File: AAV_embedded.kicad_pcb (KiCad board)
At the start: 4 copper layers, 165.8 x 114.2 mm, 51 parts, among them J1 JTAG_SWD_CONN, J10 DRV_HIGH_C2, J11 DRV_LOW_C2, J12 DRV_HIGH_C3, J13 DRV_LOW_C3, J14 DRV_LOW_C1, J2 12v in, J3 USB_C_Receptacle_USB2.0_14P, J5 THR_EN_JMP, J6 GPIO_INTERNAL_PINS, J7 GPIO_EXT_PINS, J8 Conn_01x03_Pin, J9 DRV_HIGH_C1, SW1 DAC_ADDR, SW2 IO_EXT_ADDR, SW3 SW_DIP_x03, SW4 5v_USB_EN, SW5 DAC_EN, U1 DAC101C081CIMK, U2 PCA9555D, U3 LD1117S50TR_SOT223, U4 LD1117S33TR_SOT223, U5 FXMA108

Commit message: board layout v1
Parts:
- removed 12vdecoup_H1: 0.1uF, Capacitor_SMD:C_1206_3216Metric
- removed 12vdecoup_L1: 100uF, Capacitor_SMD:C_1206_3216Metric
- removed 3.3vreg_Cin1, 5vreg_Cin2: 100nF, Capacitor_SMD:C_1206_3216Metric
- removed 3.3vreg_Cout1, 5vreg_Cout2: 10uF, Capacitor_SMD:C_1206_3216Metric
- removed D1: D_Schottky_low_forward, Diode_SMD:D_1206_3216Metric
- removed R2: 2k, Resistor_SMD:R_1206_3216Metric
- removed S1: GPTS203211B, Button_Switch_SMD:SW_Push_1P1T_NO_CK_PTS125Sx43PSMTR
- removed U4: LD1117S33TR_SOT223, Package_TO_SOT_SMD:SOT-223-3_TabPin2
- added C3: 0.1uF, Capacitor_SMD:C_1206_3216Metric, F.Cu at (134.1, 97.5)
- added C4: 0.1uF, Capacitor_SMD:C_1206_3216Metric, F.Cu at (141.6, 123.4)
- added C5: 22pF, Capacitor_SMD:C_1206_3216Metric, F.Cu at (141.8, 112.3)
- added C6: 22pF, Capacitor_SMD:C_1206_3216Metric, F.Cu at (141.5, 120.2)
- added D4: LED, LED_SMD:LED_1206_3216Metric_Pad1.42x1.75mm_HandSolder, F.Cu at (153.8, 56.0)
- added D5: LED, LED_SMD:LED_1206_3216Metric_Pad1.42x1.75mm_HandSolder, F.Cu at (162.0, 104.8)
- added D6: LED, LED_SMD:LED_1206_3216Metric_Pad1.42x1.75mm_HandSolder, F.Cu at (161.9, 94.7)
- added F2: Polyfuse_3A_15V, Fuse:Fuse_1812_4532Metric, F.Cu at (65.1, 117.3)
- added J15: Brake/FwRev, Connector_PinHeader_2.54mm:PinHeader_1x03_P2.54mm_Horizontal, F.Cu at (202.8, 148.8)
- added J16: 5v_in, TerminalBlock_MetzConnect:TerminalBlock_MetzConnect_Type011_RT05502HBWC_1x02_P5.00mm_Horizontal, F.Cu at (73.7, 50.3)
- added J17: 3.3v_in, TerminalBlock_MetzConnect:TerminalBlock_MetzConnect_Type011_RT05502HBWC_1x02_P5.00mm_Horizontal, F.Cu at (85.2, 50.3)
- added J18: 12v_in, TerminalBlock_MetzConnect:TerminalBlock_MetzConnect_Type011_RT05502HBWC_1x02_P5.00mm_Horizontal, F.Cu at (96.9, 50.3)
- added J19: ~, SparkFun-Connectors:JST-2-PTH, F.Cu at (159.2, 155.5)
- added J20: ~, SparkFun-Connectors:JST-6-SMD-1.25MM-LOCKING, F.Cu at (145.5, 155.9)
- added J21: CAN, Connector_JST:JST_EH_B2B-EH-A_1x02_P2.50mm_Vertical, F.Cu at (152.6, 95.0)
- added J23: 5v_rail, Connector_PinHeader_2.54mm:PinHeader_1x05_P2.54mm_Vertical, F.Cu at (61.7, 46.4)
- added J24: 3.3v_rail, Connector_PinHeader_2.54mm:PinHeader_1x05_P2.54mm_Vertical, F.Cu at (57.1, 46.4)
- added J25: 12v_rail, Connector_PinHeader_2.54mm:PinHeader_1x05_P2.54mm_Vertical, F.Cu at (52.5, 46.4)
- added J26: GND_rail, Connector_PinHeader_2.54mm:PinHeader_1x05_P2.54mm_Vertical, F.Cu at (66.2, 46.1)
- added J27: 12v_rail_f, Connector_PinSocket_2.54mm:PinSocket_1x05_P2.54mm_Vertical, F.Cu at (52.3, 140.2)
- added J28: 3.3v_rail_f, Connector_PinSocket_2.54mm:PinSocket_1x05_P2.54mm_Vertical, F.Cu at (56.9, 140.2)
- added J29: 5v_rail_f, Connector_PinSocket_2.54mm:PinSocket_1x05_P2.54mm_Vertical, F.Cu at (61.5, 140.2)
- added J30: GND_rail_f, Connector_PinSocket_2.54mm:PinSocket_1x05_P2.54mm_Vertical, F.Cu at (66.1, 140.2)
- added JP1: CAN_TXD_SEL, Jumper:SolderJumper-3_P1.3mm_Bridged12_Pad1.0x1.5mm, F.Cu at (154.2, 106.5)
- added JP2: CAN_RXD_SEL, Jumper:SolderJumper-3_P1.3mm_Bridged12_Pad1.0x1.5mm, F.Cu at (148.7, 106.5)
- added R11: 2k, Resistor_SMD:R_1206_3216Metric, F.Cu at (122.5, 127.4)
- added R12: 2k, Resistor_SMD:R_1206_3216Metric, F.Cu at (122.7, 131.9)
- added R13: 2k, Resistor_SMD:R_1206_3216Metric, F.Cu at (135.7, 131.1)
- added R14: 2k, Resistor_SMD:R_1206_3216Metric, F.Cu at (135.8, 136.3)
- added R25: 10k, Resistor_SMD:R_1206_3216Metric, F.Cu at (153.9, 69.0)
- added R26: 10k, Resistor_SMD:R_1206_3216Metric, F.Cu at (153.7, 58.4)
- added R27: 10k, Resistor_SMD:R_1206_3216Metric, F.Cu at (162.0, 102.4)
- added R28: 10k, Resistor_SMD:R_1206_3216Metric, F.Cu at (161.9, 97.0)
- added SW6: ~{RESET_uMOD}, Button_Switch_SMD:SW_Push_SPST_NO_Alps_SKRK, F.Cu at (131.2, 48.6)
- added SW7: ~{BOOT_uMOD}, Button_Switch_SMD:SW_Push_SPST_NO_Alps_SKRK, F.Cu at (123.7, 48.9)
- added SW8: ~{RESET_BRK}, Button_Switch_SMD:SW_Push_SPST_NO_Alps_SKRK, F.Cu at (115.8, 48.9)
- added SW9: ~{RESET_STR}, Button_Switch_SMD:SW_Push_SPST_NO_Alps_SKRK, F.Cu at (108.1, 48.9)
- added U6: MCP2515-xSO, Package_SO:SOIC-18W_7.5x11.6mm_P1.27mm, F.Cu at (152.3, 116.6)
- added U7: SN65HVD230, Package_SO:SOIC-8_3.9x4.9mm_P1.27mm, F.Cu at (142.2, 96.8)
- added Y1: 16MHz, Crystal:Crystal_HC18-U_Vertical, F.Cu at (133.5, 118.0)
- D2: value D_TVS -> LED; footprint Diode_SMD:D_1206_3216Metric -> LED_SMD:LED_1206_3216Metric_Pad1.42x1.75mm_HandSolder
- D3: footprint LED_SMD:LED_1206_3216Metric -> LED_SMD:LED_1206_3216Metric_Pad1.42x1.75mm_HandSolder
- J2: value 12v in -> Raspberry_Pi_4; footprint Connector_PinSocket_1.00mm:PinSocket_1x02_P1.00mm_Vertical -> Connector_PinSocket_2.54mm:PinSocket_2x20_P2.54mm_Vertical
- J6: value GPIO_INTERNAL_PINS -> Conn_01x07; footprint Connector_PinHeader_2.54mm:PinHeader_1x09_P2.54mm_Vertical -> Connector_PinHeader_2.54mm:PinHeader_1x07_P2.54mm_Vertical
- J7: value GPIO_EXT_PINS -> Conn_01x05; footprint Connector_PinHeader_2.54mm:PinHeader_1x13_P2.54mm_Horizontal -> Connector_PinHeader_2.54mm:PinHeader_1x05_P2.54mm_Vertical
- J8: value Conn_01x03_Pin -> Throttle Connector
- R1: value 2k -> 10k
- SW5: value DAC_EN -> THR_EN
- U3: value LD1117S50TR_SOT223 -> 74AHC1G08; footprint Package_TO_SOT_SMD:SOT-223-3_TabPin2 -> Package_TO_SOT_SMD:SOT-23-5_HandSoldering
- moved C1 117.1 mm to (183.8, 135.3), turned to 180 degrees
- moved C2 117.0 mm to (182.7, 140.8), turned to -90 degrees
- moved R3 86.1 mm to (164.6, 143.2)
- moved J1 76.5 mm to (141.9, 72.0), turned to 90 degrees
- moved U3 73.8 mm to (150.7, 86.2), turned to 180 degrees
- moved R1 70.2 mm to (161.8, 112.7), turned to 180 degrees
- moved J4 57.6 mm to (126.5, 85.1)
- moved SW4 56.7 mm to (90.1, 151.2), turned to -90 degrees
- moved SW2 54.9 mm to (116.9, 117.3), turned to -90 degrees
- moved R7 53.1 mm to (98.2, 136.3)
- moved D2 51.4 mm to (153.9, 71.5)
- moved R6 51.0 mm to (98.1, 130.9)
- moved R8 43.2 mm to (73.1, 140.7), turned to -90 degrees
- moved R5 40.2 mm to (98.2, 133.7)
- moved J2 24.4 mm to (53.8, 119.9), turned to 180 degrees
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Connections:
- net RST renamed ~{RESET_uMOD}
- D2 pad 1: Net-(D1-A) -> GND
- D2 pad 2: GND -> Net-(D2-A)
- J14 pad 1: ERR_LOW -> ERR_BRK
- J14 pad 2: ~{RST_LOW} -> ~{RST_BRK}
- J14 pad 6: TX_LOW_5v -> TX_BRK_5v
- J14 pad 7: RX_LOW_5v -> RX_DRV_5v
- J14 pad 9: 5v_reg_LOW -> 5v_reg_BRK
- J2 pad 1: GND -> Net-(J2-3V3-Pad1)
- J2 pad 2: Net-(D1-A) -> Net-(F2-Pad1)
- J4 pad 11: unconnected-(J4-~{BOOT}-Pad11) -> ~{BOOT_uMOD}
- J4 pad 17: unconnected-(J4-TX1-Pad17) -> uMod_TX1
- J4 pad 19: unconnected-(J4-RX1-Pad19) -> uMod_RX1
- J4 pad 2: Net-(J4-3.3V-Pad2) -> +3.3V
- J4 pad 20: unconnected-(J4-RX2-Pad20) -> TX_DRV_L
- J4 pad 22: unconnected-(J4-TX2-Pad22) -> RX_DRV_L
- J4 pad 40: GPIO_INTERNAL_0 -> ~{E-STOP}
- J4 pad 41: unconnected-(J4-CAN-RX-Pad41) -> CAN_RXD
- J4 pad 42: GPIO_INTERNAL_1 -> ERR_L
- J4 pad 43: unconnected-(J4-CAN-TX-Pad43) -> CAN_TXD
- J4 pad 44: GPIO_INTERNAL_2 -> ~{E-STOP-TRIG}
- J4 pad 51: SDA _MCTRL_L -> unconnected-(J4-I2C_SDA1-Pad51)
- J4 pad 53: SCL_MCTRL_L -> unconnected-(J4-I2C_SCL1-Pad53)
- J4 pad 67: ERR_HIGH_L -> GPIO_INTERNAL_8
- J4 pad 69: ERR_LOW_L -> GPIO_INTERNAL_7
- J4 pad 74: Net-(J4-3.3V-Pad2) -> +3.3V
- J4 pad 9: unconnected-(J4-USB_VIN-Pad9) -> +5V
- J6 pad 1: GPIO_INTERNAL_8 -> GPIO_INTERNAL_6
- J6 pad 2: GPIO_INTERNAL_7 -> GPIO_INTERNAL_5
- J6 pad 3: GPIO_INTERNAL_6 -> GPIO_INTERNAL_4
- J6 pad 4: GPIO_INTERNAL_5 -> GPIO_INTERNAL_3
- J6 pad 5: GPIO_INTERNAL_4 -> ~{E-STOP-TRIG}
- J6 pad 6: GPIO_INTERNAL_3 -> ERR_L
- J6 pad 7: GPIO_INTERNAL_2 -> ~{E-STOP}
- J7 pad 1: GPIO_EXT_12 -> GPIO_EXT_4
- J7 pad 2: GPIO_EXT_11 -> GPIO_EXT_3
- J7 pad 3: GPIO_EXT_10 -> GPIO_EXT_2
- J7 pad 4: GPIO_EXT_9 -> GPIO_EXT_1
- J7 pad 5: GPIO_EXT_8 -> GPIO_EXT_0
- J9 pad 1: ERR_HIGH -> ERR_STR
- J9 pad 2: ~{RST_HIGH} -> ~{RST_STR}
- J9 pad 6: TX_HIGH_5v -> TX_STR_5v
- J9 pad 7: RX_HIGH_5v -> RX_DRV_5v
- J9 pad 9: 5v_reg_HIGH -> 5v_reg_STR
- R1 pad 1: +5V -> GND
- R1 pad 2: SCL_1_H -> Net-(U6-~{RESET})
- U2 pad 15: GPIO_EXT_7 -> ~{RST_STR}
- U2 pad 16: GPIO_EXT_8 -> ~{RST_BRK}
- U3 pad 1: GND -> TX_BRK_5v
- U3 pad 2: +5V -> TX_STR_5v
- U3 pad 3: +12v -> GND
- U5 pad 12: unconnected-(U5-B7-Pad12) -> RX_DRV_5v
- U5 pad 13: unconnected-(U5-B6-Pad13) -> TX_DRV_5v
- U5 pad 14: unconnected-(U5-B5-Pad14) -> ERR_STR
- U5 pad 15: ERR_HIGH -> ERR_BRK
- U5 pad 16: ERR_LOW -> ~{ERR}
- U5 pad 5: ERR_LOW_L -> ~{E-STOP}
- U5 pad 6: ERR_HIGH_L -> ERR_BRK_L
- U5 pad 7: unconnected-(U5-A5-Pad7) -> ERR_STR_L
- U5 pad 8: unconnected-(U5-A6-Pad8) -> TX_DRV_L
- U5 pad 9: unconnected-(U5-A7-Pad9) -> RX_DRV_L
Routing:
- net ~{E-STOP}: track 0.00 -> 186.2 mm, vias 0 -> 8
- net ~{RST_BRK}: track 0.00 -> 169.4 mm, vias 0 -> 4
- net ~{RST_STR}: track 0.00 -> 159.5 mm, vias 0 -> 2
- net ~{RESET_uMOD}: track 0.00 -> 156.7 mm, vias 0 -> 3
- net +12V: track 0.00 -> 150.5 mm
- net ~{E-STOP-TRIG}: track 0.00 -> 129.0 mm, vias 0 -> 6
- net CAN_SCK: track 0.00 -> 121.9 mm, vias 0 -> 1
- net CAN_MISO: track 0.00 -> 112.7 mm, vias 0 -> 1
- net CAN_MOSI: track 0.00 -> 112.3 mm, vias 0 -> 1
- net CAN_CS: track 0.00 -> 109.8 mm, vias 0 -> 1
- net ERR_STR: track 0.00 -> 109.6 mm
- net Fw/Rv: track 0.00 -> 106.1 mm
- net Brk_low: track 0.00 -> 105.0 mm, vias 0 -> 1
- net Brk_hi: track 0.00 -> 104.2 mm, vias 0 -> 2
- net GPIO_INTERNAL_3: track 20.5 -> 121.4 mm, vias 0 -> 6
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- added copper zone on F.Cu, net +12V
- added copper zone on B.Cu, net +3.3V
- added copper zone on In2.Cu, net +5V
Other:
- board size 165.8 x 114.2 mm -> 168.2 x 114.7 mm
- board text added: "+5v"
- board text added: "12v"
- board text added: "3.3v"
- board text added: "DAC Vin | SW1 | SW2 | SW3 | Vout| -----------------| | 0 | 0 | 0 | 5V | | 0 | 0 | 1 | 4.54V | | 0 | 1 | 0 | 4V | | 0 | 1 | 1 | 3.7V | | 1 | 0 | 0 | 3.12V | | 1 | 0 | 1 | 3.33V | | 1 | 1 | 0 | 2.85V | | 1 | 1 | 1 | 2.7V |"
- board text added: "GND"
- board text added: "Motor Controller"
- board text added: "Only enable when board is not powered."
- board text added: "RASPBERRY PI"
- board text added: "SW1^ SW2^ SW3^"
- board text removed: "Internal GPIO"
- board text removed: "THROTTLE"

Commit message: add solder jumpers
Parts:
- added JP3: tx_sel, Jumper:SolderJumper-3_P1.3mm_Bridged12_Pad1.0x1.5mm, F.Cu at (126.2, 74.3)
- added JP4: rx_sel, Jumper:SolderJumper-3_P1.3mm_Bridged12_Pad1.0x1.5mm, F.Cu at (118.6, 73.0)
- Y1: footprint Crystal:Crystal_HC18-U_Vertical -> Crystal:Crystal_HC49-4H_Vertical
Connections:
- J4 pad 20: TX_DRV_L -> Net-(J4-RX2)
- J4 pad 22: RX_DRV_L -> Net-(J4-TX2)
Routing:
- net Net-(J4-RX2): track 0.00 -> 19.1 mm, vias 0 -> 2
- net unconnected-(J3-SHIELD-PadS1): track 0.00 -> 15.7 mm
- net RX_DRV_L: track 78.5 -> 91.9 mm, vias 4 -> 6
- net GPIO_INTERNAL_4: track 118.7 -> 130.2 mm, vias 4 -> 6
- net Net-(J4-TX2): track 0.00 -> 9.93 mm, vias 0 -> 2
- net GPIO_INTERNAL_3: track 121.4 -> 130.6 mm, vias 6 -> 8
- net TX_DRV_L: track 76.3 -> 81.4 mm, vias 4 -> 6
- net DAC_THR: track 132.8 -> 135.7 mm
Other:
- board text added: "Rev. 1"
- board text added: "Throttle enable"
- board text added: "i2c io expander address select"

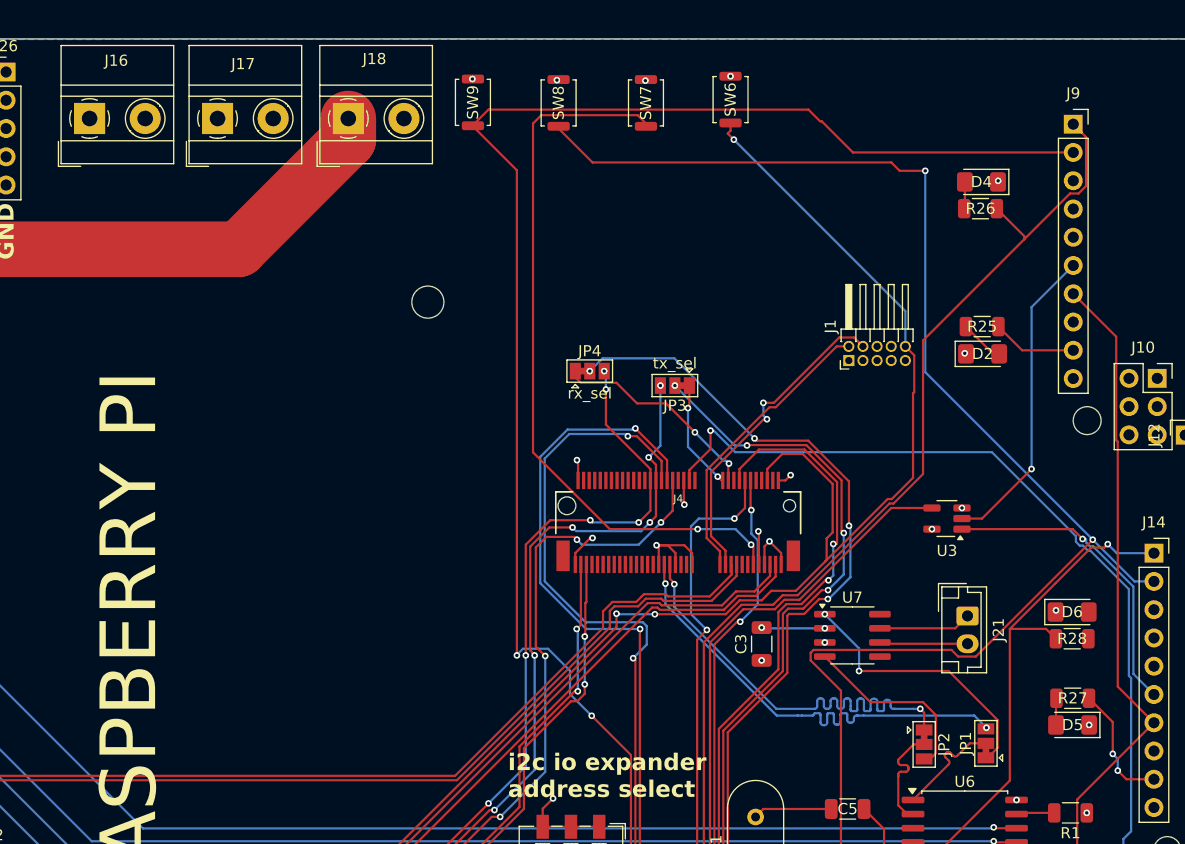
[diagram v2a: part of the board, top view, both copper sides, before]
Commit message: add more silkscreen
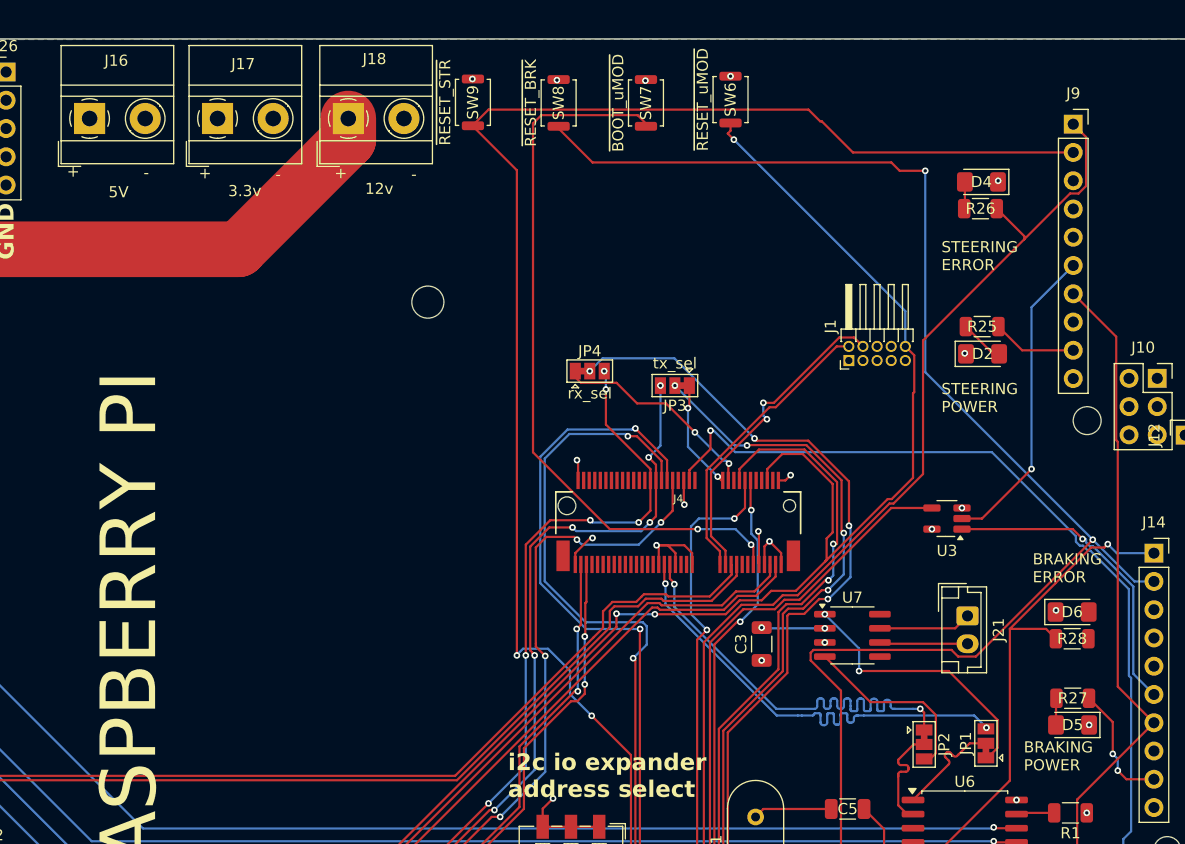
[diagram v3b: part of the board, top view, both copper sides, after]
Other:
- board text added: "+"
- board text added: "-"
- board text added: "5V"
- board text added: "BRAKING ERROR"
- board text added: "BRAKING POWER"
- board text added: "STEERING ERROR"
- board text added: "STEERING POWER"
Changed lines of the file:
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@@
 		(property "Value" "~{RESET_uMOD}"
 			(at 0 2.5 90)
-			(layer "F.Fab")
+			(layer "F.SilkS")
 			(effects
 				(font
@@
 		(property "Value" "~{BOOT_uMOD}"
 			(at 0 2.5 90)
-			(layer "F.Fab")
+			(layer "F.SilkS")
 			(effects
 				(font
@@
 		(property "Value" "~{RESET_BRK}"
 			(at 0 2.5 90)
-			(layer "F.Fab")
+			(layer "F.SilkS")
 			(effects
 				(font
@@
 		(property "Value" "~{RESET_STR}"
 			(at 0 2.5 90)
-			(layer "F.Fab")
+			(layer "F.SilkS")
 			(effects
 				(font
@@
 		(layer "Edge.Cuts")
 	)
+	(gr_text "12v"
+		(at 98.4 57.2 0)
+		(layer "F.SilkS")
+		(effects
+			(font
+				(size 1 1)
+				(thickness 0.1)
+			)
+			(justify left bottom)
+		)
+	)
+	(gr_text "BRAKING\nERROR"
+		(at 158.4 92.1 0)
+		(layer "F.SilkS")
+		(effects
+			(font
+				(size 1 1)
+				(thickness 0.1)
+			)
+			(justify left bottom)
+		)
+	)
 	(gr_text "3.3v"
 		(at 57.6 63.1 90)
@@
 		)
 	)
+	(gr_text "5V"
+		(at 75.35 57.5 0)
+		(layer "F.SilkS")
+		(effects
+			(font
+				(size 1 1)
+				(thickness 0.1)
+			)
+			(justify left bottom)
+		)
+	)
 	(gr_text "External i2c GPIO"
 		(at 96.9 149.3 0)
@@
 		)
 	)
+	(gr_text "-"
+		(at 90.35 55.9 0)
+		(layer "F.SilkS")
+		(effects
+			(font
+				(size 1 1)
+				(thickness 0.1)
+			)
+			(justify left bottom)
+		)
+	)
+	(gr_text "-"
+		(at 102.55 55.9 0)
+		(layer "F.SilkS")
+		(effects
+			(font
+				(size 1 1)
+				(thickness 0.1)
+			)
+			(justify left bottom)
+		)
+	)
 	(gr_text "12v"
 		(at 52.8 157.05 90)
@@
 		)
 	)
+	(gr_text "+"
+		(at 95.65 55.8 0)
+		(layer "F.SilkS")
+		(effects
+			(font
+				(size 1 1)
+				(thickness 0.1)
+			)
+			(justify left bottom)
+		)
+	)
 	(gr_text "3.3v"
 		(at 57.9 157.1 90)
@@
 		)
 	)
+	(gr_text "+"
+		(at 83.45 55.8 0)
+		(layer "F.SilkS")
+		(effects
+			(font
+				(size 1 1)
+				(thickness 0.1)
+			)
+			(justify left bottom)
+		)
+	)
 	(gr_text "GND"
 		(at 67 63 90)
@@
 		)
 	)
+	(gr_text "-"
+		(at 78.5 55.75 0)
+		(layer "F.SilkS")
+		(effects
+			(font
+				(size 1 1)
+				(thickness 0.1)
+			)
+			(justify left bottom)
+		)
+	)
+	(gr_text "STEERING\nPOWER"
+		(at 150.2 76.8 0)
+		(layer "F.SilkS")
+		(effects
+			(font
+				(size 1 1)
+				(thickness 0.1)
+			)
+			(justify left bottom)
+		)
+	)
 	(gr_text "RASPBERRY PI"
 		(at 80.15 121.95 90)
@@
 		)
 	)
+	(gr_text "BRAKING\nPOWER"
+		(at 157.6 109 0)
+		(layer "F.SilkS")
+		(effects
+			(font
+				(size 1 1)
+				(thickness 0.1)
+			)
+			(justify left bottom)
+		)
+	)
 	(gr_text "Motor\nController"
 		(at 190.65 129.55 0)
@@
 		)
 	)
+	(gr_text "3.3v"
+		(at 86.1 57.4 0)
+		(layer "F.SilkS")
+		(effects
+			(font
+				(size 1 1)
+				(thickness 0.1)
+			)
+			(justify left bottom)
+		)
+	)
 	(gr_text "BRAKING \nACTUATOR"
 		(at 212.45 114.75 90)
@@
 		)
 	)
+	(gr_text "+"
+		(at 71.6 55.65 0)
+		(layer "F.SilkS")
+		(effects
+			(font
+				(size 1 1)
+				(thickness 0.1)
+			)
+			(justify left bottom)
+		)
+	)
 	(gr_text "12v"
 		(at 52.5 63.05 90)
@@
 		(layer "F.SilkS")
 		(effects
+			(font
+				(size 1 1)
+				(thickness 0.1)
+			)
+			(justify left bottom)
+		)
+	)
+	(gr_text "STEERING \nERROR"
+		(at 150.2 64.05 0)
+		(layer "F.SilkS")
+		(effects

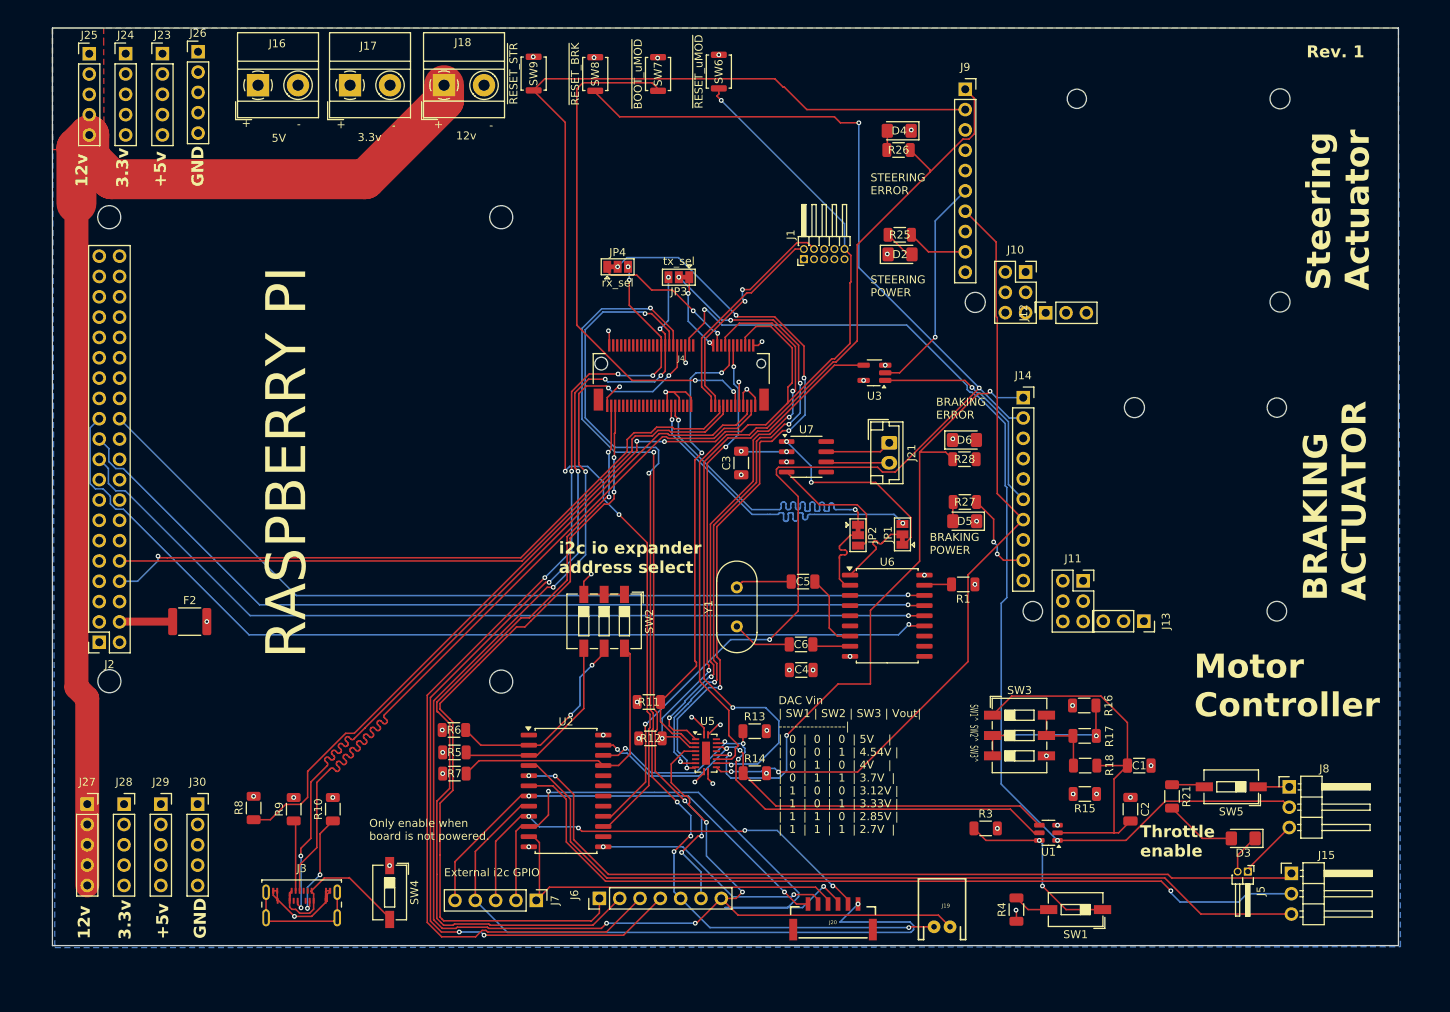
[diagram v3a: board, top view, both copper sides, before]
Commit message: added mounting holes
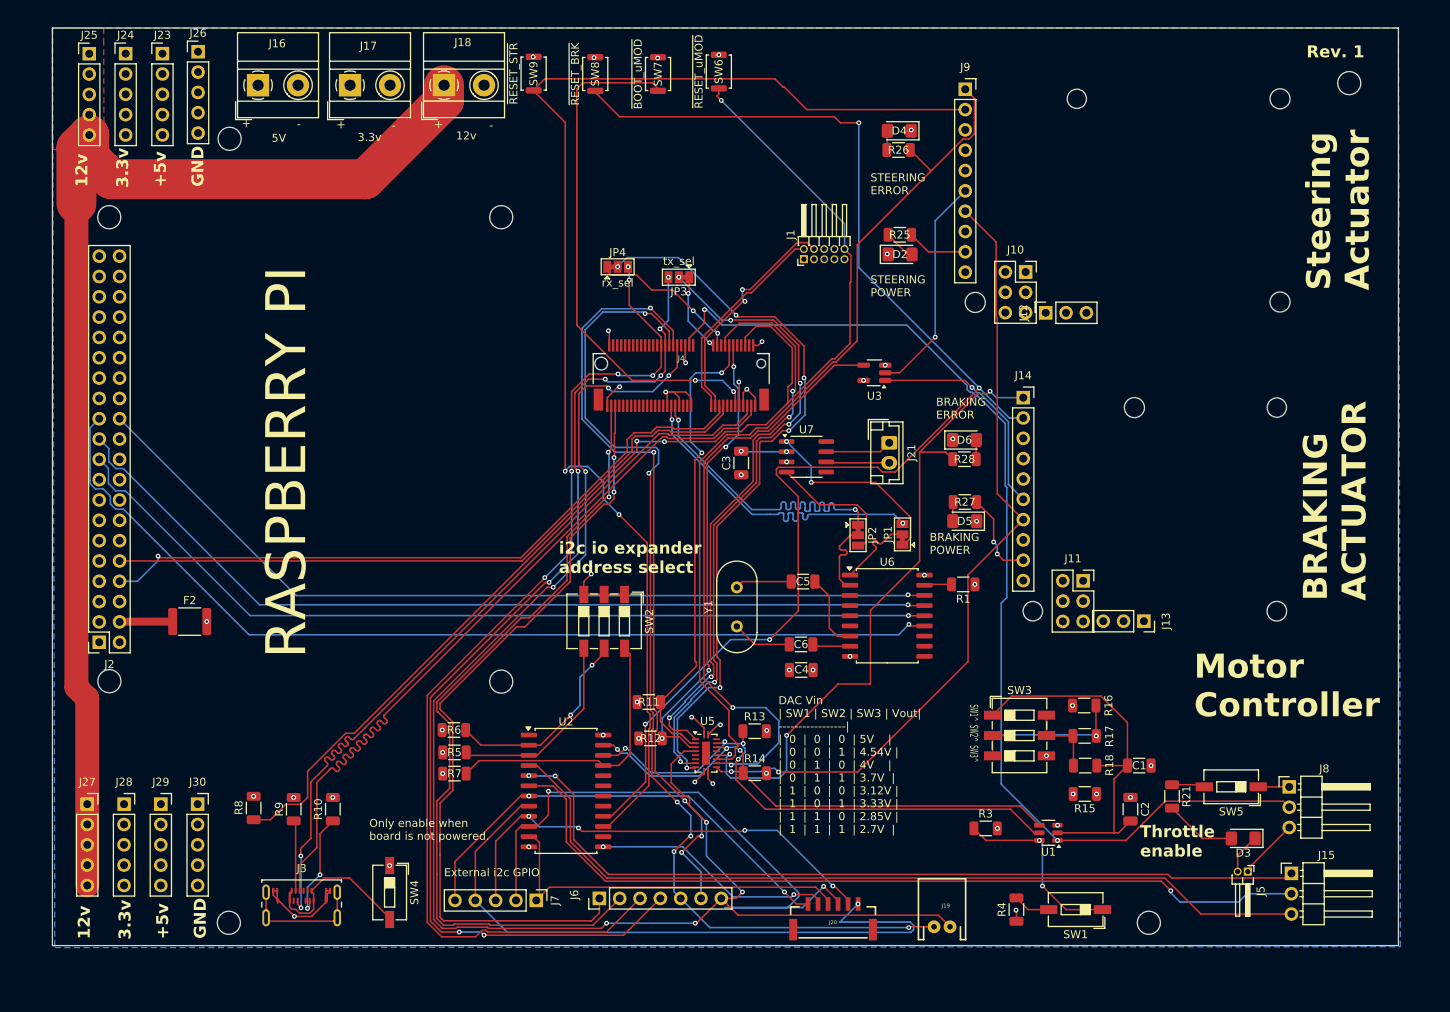
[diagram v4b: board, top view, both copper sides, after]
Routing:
- net Net-(D6-A): track 0.00 -> 2.41 mm
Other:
- outline, holes or cut-outs redrawn
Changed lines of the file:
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@@
 	)
 	(gr_circle
+		(center 185 155)
+		(end 186.332904 154.45)
+		(stroke
+			(width 0.05)
+			(type default)
+		)
+		(fill none)
+		(layer "Edge.Cuts")
+	)
+	(gr_circle
+		(center 210.05 50.041919)
+		(end 211.382904 49.491919)
+		(stroke
+			(width 0.05)
+			(type default)
+		)
+		(fill none)
+		(layer "Edge.Cuts")
+	)
+	(gr_circle
 		(center 104.05 124.85)
 		(end 105.382904 124.3)
@@
 	)
 	(gr_circle
+		(center 70 155)
+		(end 71.332904 154.45)
+		(stroke
+			(width 0.05)
+			(type default)
+		)
+		(fill none)
+		(layer "Edge.Cuts")
+	)
+	(gr_circle
 		(center 104.05 66.8)
 		(end 105.382904 66.25)
@@
 		(layer "Edge.Cuts")
 	)
+	(gr_circle
+		(center 70.1 57)
+		(end 71.432904 56.45)
+		(stroke
+			(width 0.05)
+			(type default)
+		)
+		(fill none)
+		(layer "Edge.Cuts")
+	)
 	(gr_rect
 		(start 47.95 43.15)
@@
 	)
 	(segment
+		(start 163.4125 94.675)
+		(end 163.4375 94.65)
+		(width 0.2)
+		(layer "F.Cu")
+		(net 183)
+	)
+	(segment
+		(start 163.4125 97.05)
+		(end 163.4125 94.675)
+		(width 0.2)
+		(layer "F.Cu")
+		(net 183)
+	)
+	(segment
